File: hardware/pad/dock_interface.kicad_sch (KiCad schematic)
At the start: 6 parts, among them J1 Pogo_6p, U1 TPD4E1U06DBVR

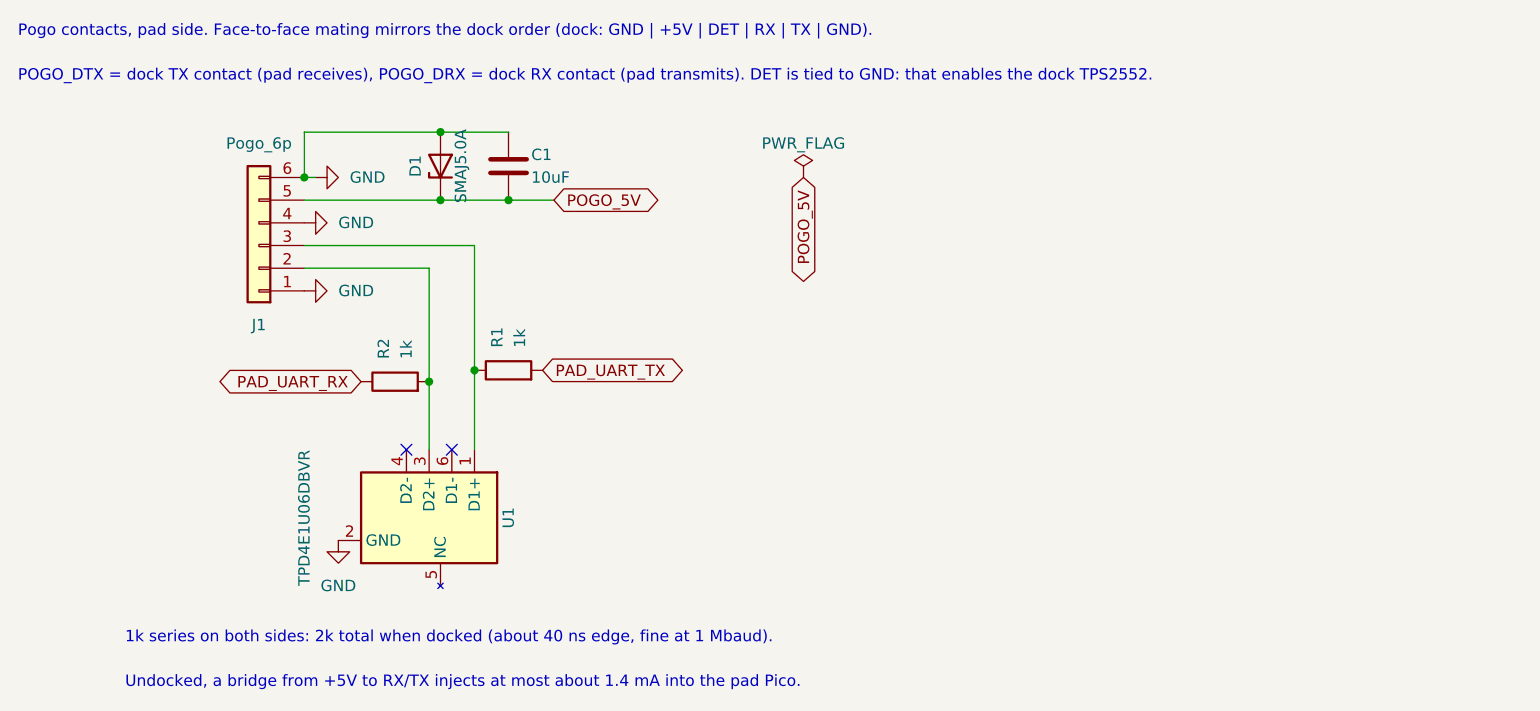
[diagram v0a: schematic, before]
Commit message: Pad: display on 9-pin JST-PH with backlight MOSFET (GP27), pogo cable connector; pogo board schematic; guide updated to final refs
Co-Authored-By: Claude Opus 5.5 <noreply@anthropic.com>
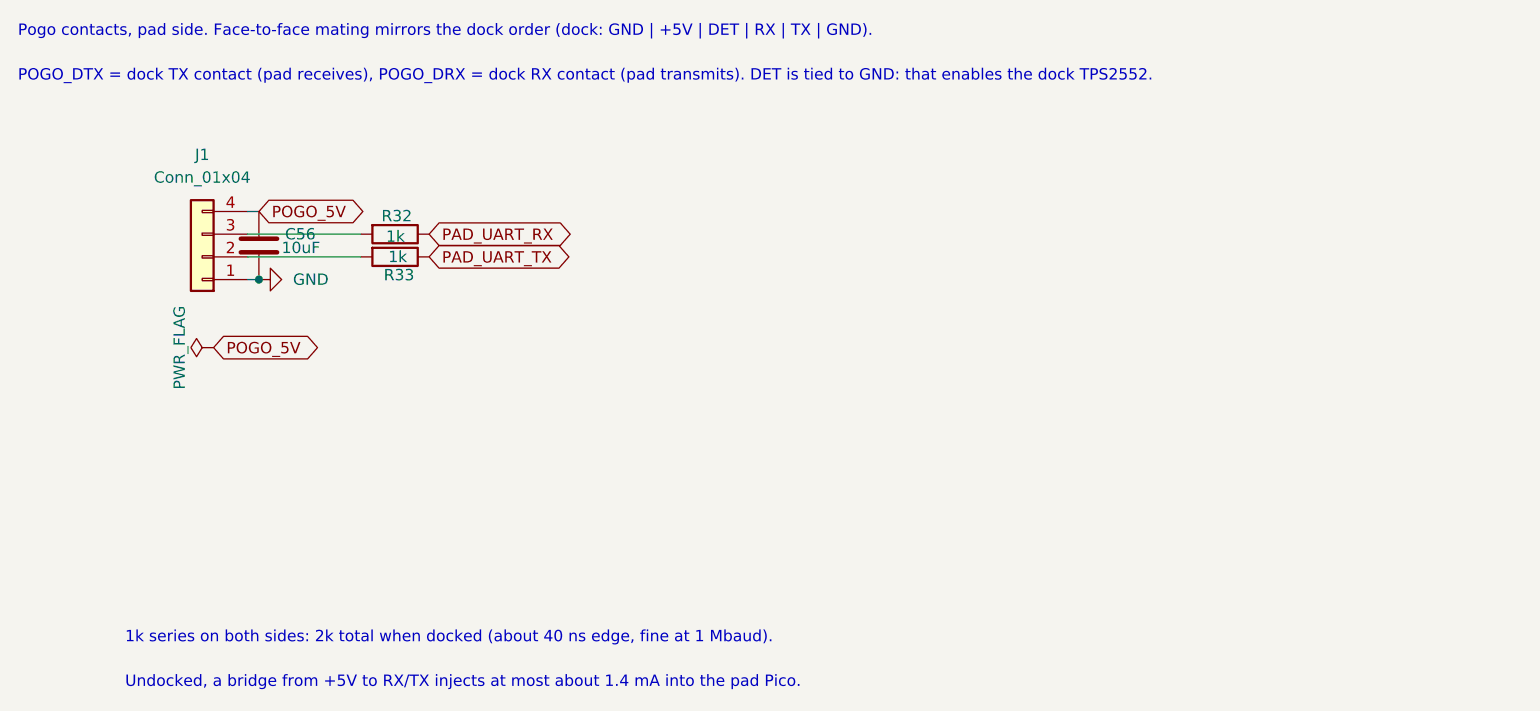
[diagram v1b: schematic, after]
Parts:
- removed C1: 10uF, Capacitor_SMD:C_0805_2012Metric_Pad1.18x1.45mm_HandSolder, symbol Device:C
- removed D1: SMAJ5.0A, Diode_SMD:D_SMA, symbol Device:D_Zener
- removed J1: Pogo_6p, dock:Pogo-6, symbol Connector_Generic:Conn_01x06
- removed R1, R2: 1k, Resistor_SMD:R_0805_2012Metric_Pad1.20x1.40mm_HandSolder, symbol Device:R
- removed U1: TPD4E1U06DBVR, Package_TO_SOT_SMD:SOT-23-6, symbol pad_custom:TPD4E1U06DBV
- added C56: 10uF, Capacitor_SMD:C_0805_2012Metric_Pad1.18x1.45mm_HandSolder, symbol Device:C
- added J1: Conn_01x04, Connector_JST:JST_XH_B4B-XH-A_1x04_P2.50mm_Vertical, symbol Connector_Generic:Conn_01x04
- added R32, R33: 1k, Resistor_SMD:R_0805_2012Metric_Pad1.20x1.40mm_HandSolder, symbol Device:R
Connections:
- net GND: now also C56.1, J1.1 (Pin_1)
- net PAD_UART_RX: now also R32.1
- net PAD_UART_TX: now also R33.1
- net POGO_5V: now also C56.2, J1.4 (Pin_4)
- new net: J1.2 (Pin_2), R33.2
- new net: J1.3 (Pin_3), R32.2
- no-connect marks 2 -> 0

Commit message: Pad PCB: first placement; SWD header removed, side-entry JST connectors, new footprints
- J4 (SWD) removed; A1 on the NoSWD Pico socket footprint (holes would sit under key 5)
- J1/J7/J2/J3 side-entry JST (S*B), J5 stays vertical
- New footprints: PEC11R encoder (13.2 mm lugs), SOIC-8-1EP hand-solder (TP4056),
  narrower SOT-563 pads
- All footprints placed on the 100 x 92 board; ring LEDs radial at R 12.7,
  encoders at 16.6 / 83.4; edge clearance rule 0.2 mm
- PCB_PLACEMENT.md and placement drawings in docs/

Co-Authored-By: Claude Opus 5.5 <noreply@anthropic.com>
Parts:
- J1: footprint Connector_JST:JST_XH_B4B-XH-A_1x04_P2.50mm_Vertical -> Connector_JST:JST_XH_S4B-XH-A_1x04_P2.50mm_Horizontal
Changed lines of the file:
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@@
 			)
 		)
-		(property "Footprint" "Connector_JST:JST_XH_B4B-XH-A_1x04_P2.50mm_Vertical"
+		(property "Footprint" "Connector_JST:JST_XH_S4B-XH-A_1x04_P2.50mm_Horizontal"
 			(at 40.64 44.45 0)
 			(hide yes)
